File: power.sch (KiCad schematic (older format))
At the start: 51 parts, among them U1 LFE5U-12F-8BG256C, U13 TLV62569DBVR, U14 TLV62569DBVR, U15 TLV62569DBVR

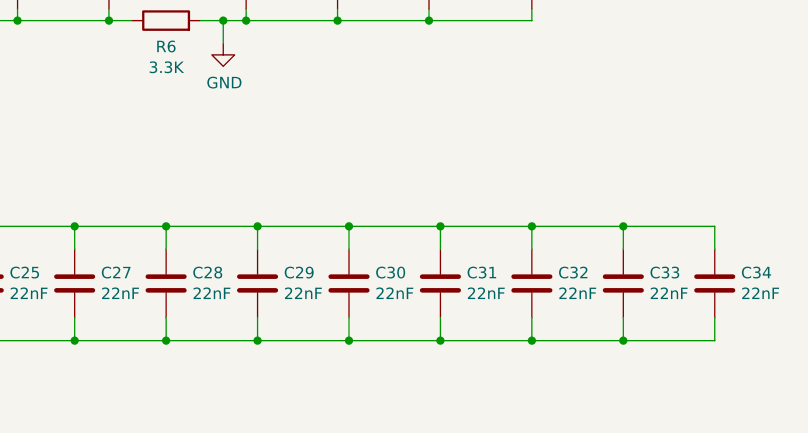
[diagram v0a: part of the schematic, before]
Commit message: add hdmi output
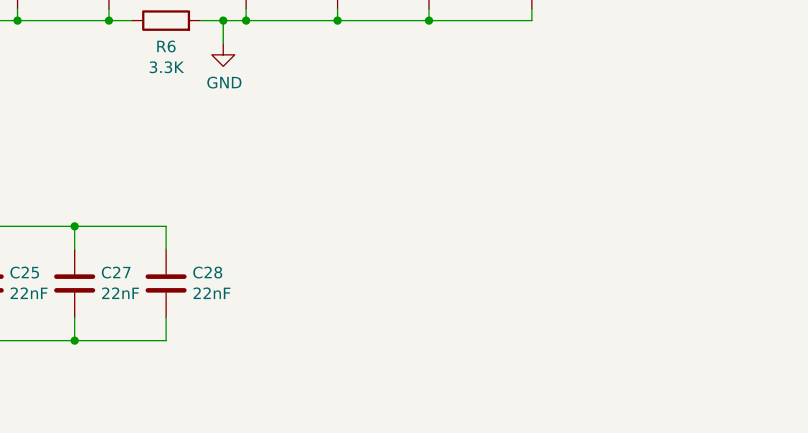
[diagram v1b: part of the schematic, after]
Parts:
- removed C29, C30, C31, C32, C33, C34: 22nF, Capacitor_SMD:C_0402_1005Metric, symbol Device:C
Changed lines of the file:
@@
 $Descr A4 11693 8268
 encoding utf-8
-Sheet 5 7
+Sheet 5 8
 Title ""
 Date ""
@@
 $EndComp
 $Comp
-L Device:C C11
-U 1 1 5C3D9514
-P 9250 3500
-F 0 "C11" H 9365 3546 50  0000 L CNN
-F 1 "22uF" H 9365 3455 50  0000 L CNN
-F 2 "Capacitor_SMD:C_0805_2012Metric" H 9288 3350 50  0001 C CNN
-F 3 "~" H 9250 3500 50  0001 C CNN
-	1    9250 3500
-	1    0    0    -1
-$EndComp
-$Comp
 L Device:C C14
 U 1 1 5C3D951A
@@
 	1    0    0    -1
 $EndComp
-$Comp
-L Device:C C17
-U 1 1 5C3D9520
-P 10100 3500
-F 0 "C17" H 10215 3546 50  0000 L CNN
-F 1 "2.2uF" H 10215 3455 50  0000 L CNN
-F 2 "Capacitor_SMD:C_0603_1608Metric" H 10138 3350 50  0001 C CNN
-F 3 "~" H 10100 3500 50  0001 C CNN
-	1    10100 3500
-	1    0    0    -1
-$EndComp
 Wire Wire Line
 	8650 3700 8750 3700
-Wire Wire Line
-	10100 3700 10100 3650
-Wire Wire Line
-	9250 3650 9250 3700
-Connection ~ 9250 3700
-Wire Wire Line
-	9250 3700 9650 3700
 Wire Wire Line
 	9650 3650 9650 3700
@@
 Connection ~ 8850 3700
 Wire Wire Line
-	8850 3700 9250 3700
-Wire Wire Line
 	8750 3800 8750 3700
 Connection ~ 8750 3700
@@
 Wire Wire Line
 	8250 3300 8850 3300
-Wire Wire Line
-	10100 3300 10100 3350
 Connection ~ 8250 3300
 Wire Wire Line
@@
 	9650 3300 10100 3300
 Wire Wire Line
-	9250 3350 9250 3300
-Connection ~ 9250 3300
-Wire Wire Line
-	9250 3300 9650 3300
-Wire Wire Line
 	8850 3350 8850 3300
 Connection ~ 8850 3300
-Wire Wire Line
-	8850 3300 9250 3300
 Wire Wire Line
 	10100 3300 10100 3200
@@
 $EndComp
 $Comp
-L Device:C C29
-U 1 1 5C2DC744
-P 8900 6150
-F 0 "C29" H 9015 6196 50  0000 L CNN
-F 1 "22nF" H 9015 6105 50  0000 L CNN
-F 2 "Capacitor_SMD:C_0402_1005Metric" H 8938 6000 50  0001 C CNN
-F 3 "~" H 8900 6150 50  0001 C CNN
-	1    8900 6150
-	1    0    0    -1
-$EndComp
-$Comp
-L Device:C C30
-U 1 1 5C2DC74A
-P 9300 6150
-F 0 "C30" H 9415 6196 50  0000 L CNN
-F 1 "22nF" H 9415 6105 50  0000 L CNN
-F 2 "Capacitor_SMD:C_0402_1005Metric" H 9338 6000 50  0001 C CNN
-F 3 "~" H 9300 6150 50  0001 C CNN
-	1    9300 6150
-	1    0    0    -1
-$EndComp
-$Comp
-L Device:C C31
-U 1 1 5C2E40D1
-P 9700 6150
-F 0 "C31" H 9815 6196 50  0000 L CNN
-F 1 "22nF" H 9815 6105 50  0000 L CNN
-F 2 "Capacitor_SMD:C_0402_1005Metric" H 9738 6000 50  0001 C CNN
-F 3 "~" H 9700 6150 50  0001 C CNN
-	1    9700 6150
-	1    0    0    -1
-$EndComp
-$Comp
-L Device:C C32
-U 1 1 5C2E40D7
-P 10100 6150
-F 0 "C32" H 10215 6196 50  0000 L CNN
-F 1 "22nF" H 10215 6105 50  0000 L CNN
-F 2 "Capacitor_SMD:C_0402_1005Metric" H 10138 6000 50  0001 C CNN
-F 3 "~" H 10100 6150 50  0001 C CNN
-	1    10100 6150
-	1    0    0    -1
-$EndComp
-$Comp
-L Device:C C33
-U 1 1 5C2E40DD
-P 10500 6150
-F 0 "C33" H 10615 6196 50  0000 L CNN
-F 1 "22nF" H 10615 6105 50  0000 L CNN
-F 2 "Capacitor_SMD:C_0402_1005Metric" H 10538 6000 50  0001 C CNN
-F 3 "~" H 10500 6150 50  0001 C CNN
-	1    10500 6150
-	1    0    0    -1
-$EndComp
-$Comp
-L Device:C C34
-U 1 1 5C2E40E3
-P 10900 6150
-F 0 "C34" H 11015 6196 50  0000 L CNN
-F 1 "22nF" H 11015 6105 50  0000 L CNN
-F 2 "Capacitor_SMD:C_0402_1005Metric" H 10938 6000 50  0001 C CNN
-F 3 "~" H 10900 6150 50  0001 C CNN
-	1    10900 6150
-	1    0    0    -1
-$EndComp
-$Comp
 L power:+3V3 #PWR0146
 U 1 1 5C2EB891
@@
 	6500 5900 6900 5900
 Wire Wire Line
-	10900 5900 10900 6000
-Wire Wire Line
-	10900 6300 10900 6400
-Wire Wire Line
-	10900 6400 10500 6400
-Wire Wire Line
 	6500 6400 6500 6300
 Wire Wire Line
@@
 Wire Wire Line
 	8500 6300 8500 6400
-Connection ~ 8500 6400
 Wire Wire Line
 	8500 6400 8100 6400
 Wire Wire Line
-	8900 6300 8900 6400
-Connection ~ 8900 6400
-Wire Wire Line
-	8900 6400 8500 6400
-Wire Wire Line
-	9300 6300 9300 6400
-Connection ~ 9300 6400
-Wire Wire Line
-	9300 6400 8900 6400
-Wire Wire Line
-	9700 6300 9700 6400
-Connection ~ 9700 6400
-Wire Wire Line
-	9700 6400 9300 6400
-Wire Wire Line
-	10100 6300 10100 6400
-Connection ~ 10100 6400
-Wire Wire Line
-	10100 6400 9700 6400
-Wire Wire Line
-	10500 6300 10500 6400
-Connection ~ 10500 6400
-Wire Wire Line
-	10500 6400 10100 6400
-Wire Wire Line
-	10500 6000 10500 5900
-Connection ~ 10500 5900
-Wire Wire Line
-	10500 5900 10900 5900
-Wire Wire Line
-	10100 6000 10100 5900
-Connection ~ 10100 5900
-Wire Wire Line
-	10100 5900 10500 5900
-Wire Wire Line
-	9700 6000 9700 5900
-Connection ~ 9700 5900
-Wire Wire Line
-	9700 5900 10100 5900
-Wire Wire Line
-	9300 6000 9300 5900
-Connection ~ 9300 5900
-Wire Wire Line
-	9300 5900 9700 5900
-Wire Wire Line
-	8900 6000 8900 5900
-Connection ~ 8900 5900
-Wire Wire Line
-	8900 5900 9300 5900
-Wire Wire Line
 	8500 6000 8500 5900
-Connection ~ 8500 5900
-Wire Wire Line
-	8500 5900 8900 5900
 Wire Wire Line
 	8100 6000 8100 5900
@@
 	1    0    0    -1
 $EndComp
+Wire Wire Line
+	8850 3300 9250 3300
+Wire Wire Line
+	9250 3300 9650 3300
+Connection ~ 9250 3300
+Wire Wire Line
+	9250 3350 9250 3300
+Wire Wire Line
+	8850 3700 9250 3700
+Wire Wire Line
+	9250 3700 9650 3700
+Connection ~ 9250 3700
+Wire Wire Line
+	9250 3650 9250 3700
+$Comp
+L Device:C C11
+U 1 1 5C3D9514
+P 9250 3500
+F 0 "C11" H 9365 3546 50  0000 L CNN
+F 1 "22uF" H 9365 3455 50  0000 L CNN
+F 2 "Capacitor_SMD:C_0805_2012Metric" H 9288 3350 50  0001 C CNN
+F 3 "~" H 9250 3500 50  0001 C CNN
+	1    9250 3500
+	1    0    0    -1
+$EndComp
+Wire Wire Line
+	10100 3300 10100 3350
+Wire Wire Line
+	10100 3700 10100 3650
+$Comp
+L Device:C C17
+U 1 1 5C3D9520
+P 10100 3500
+F 0 "C17" H 10215 3546 50  0000 L CNN
+F 1 "2.2uF" H 10215 3455 50  0000 L CNN
+F 2 "Capacitor_SMD:C_0603_1608Metric" H 10138 3350 50  0001 C CNN
+F 3 "~" H 10100 3500 50  0001 C CNN
+	1    10100 3500
+	1    0    0    -1
+$EndComp
